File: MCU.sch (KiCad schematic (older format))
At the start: 14 parts

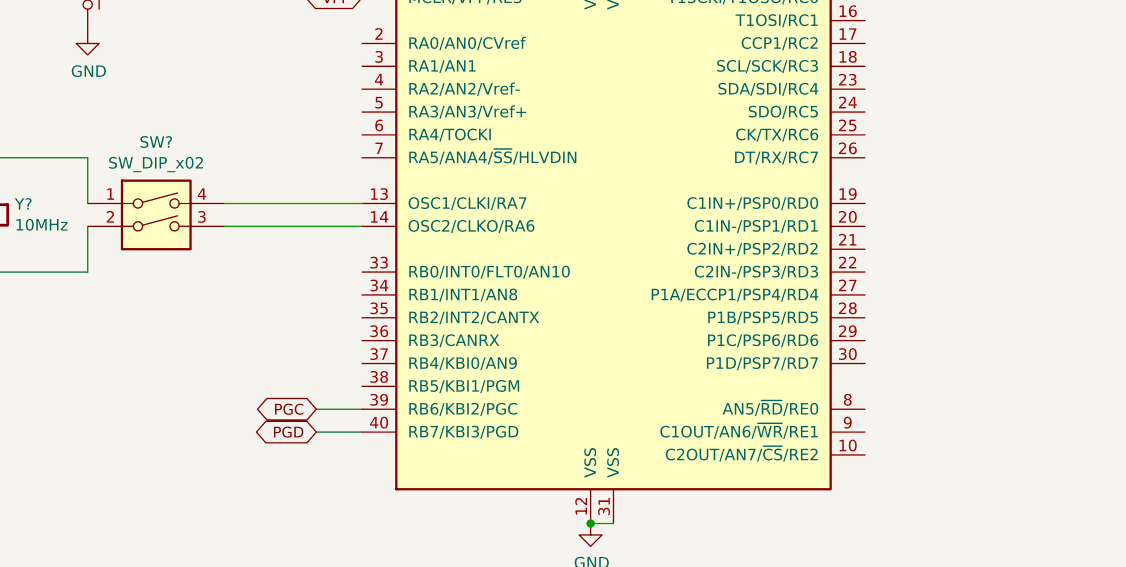
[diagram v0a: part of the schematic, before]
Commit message: LCD Blok Tasarımı
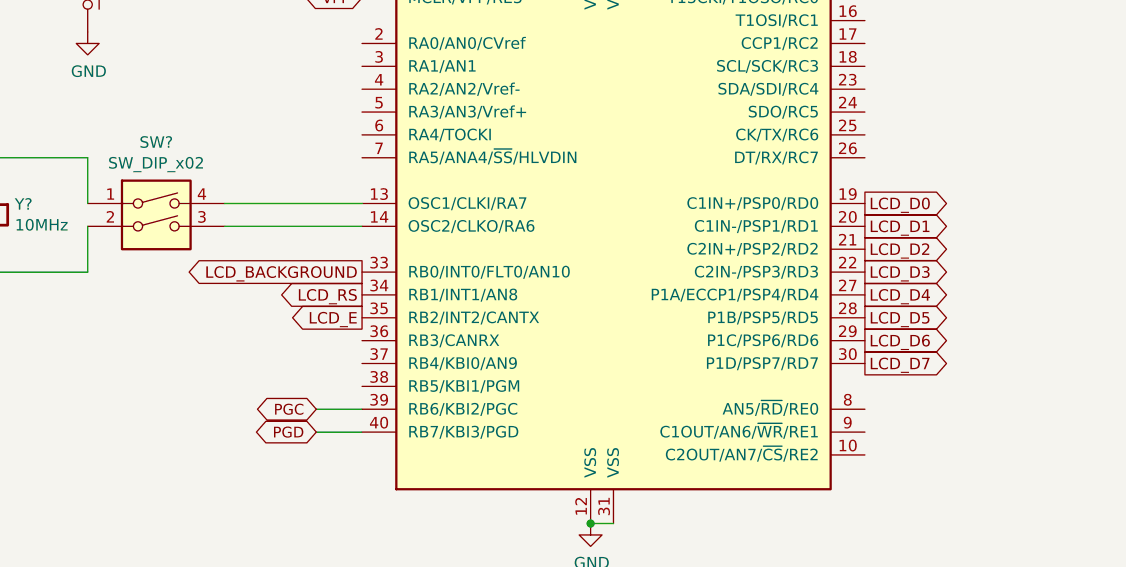
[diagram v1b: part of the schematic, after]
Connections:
- net LCD_D0: now reaches U?.19 (C1IN+/PSP0/RD0)
- net LCD_D1: now reaches U?.20 (C1IN-/PSP1/RD1)
- net LCD_D2: now reaches U?.21 (C2IN+/PSP2/RD2)
- net LCD_D3: now reaches U?.22 (C2IN-/PSP3/RD3)
- net LCD_D4: now reaches U?.27 (P1A/ECCP1/PSP4/RD4)
- net LCD_D5: now reaches U?.28 (P1B/PSP5/RD5)
- net LCD_D6: now reaches U?.29 (P1C/PSP6/RD6)
- net LCD_D7: now reaches U?.30 (P1D/PSP7/RD7)
- net LCD_BACKGROUND: now reaches U?.33 (RB0/INT0/FLT0/AN10)
- net LCD_RS: now reaches U?.34 (RB1/INT1/AN8)
- net LCD_E: now reaches U?.35 (RB2/INT2/CANTX)
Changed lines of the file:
@@
 $Descr A4 11693 8268
 encoding utf-8
-Sheet 2 2
+Sheet 2 3
 Title ""
 Date ""
@@
 	3350 2850 3300 2850
 Connection ~ 3300 2850
+Text GLabel 4500 4350 0    50   Output ~ 0
+LCD_BACKGROUND
+Text GLabel 4500 4450 0    50   Output ~ 0
+LCD_RS
+Text GLabel 4500 4550 0    50   Output ~ 0
+LCD_E
+Text GLabel 6700 4050 2    50   Output ~ 0
+LCD_D0
+Text GLabel 6700 4150 2    50   Output ~ 0
+LCD_D1
+Text GLabel 6700 4250 2    50   Output ~ 0
+LCD_D2
+Text GLabel 6700 4350 2    50   Output ~ 0
+LCD_D3
+Text GLabel 6700 4450 2    50   Output ~ 0
+LCD_D4
+Text GLabel 6700 4550 2    50   Output ~ 0
+LCD_D5
+Text GLabel 6700 4650 2    50   Output ~ 0
+LCD_D6
+Text GLabel 6700 4750 2    50   Output ~ 0
+LCD_D7
 $EndSCHEMATC

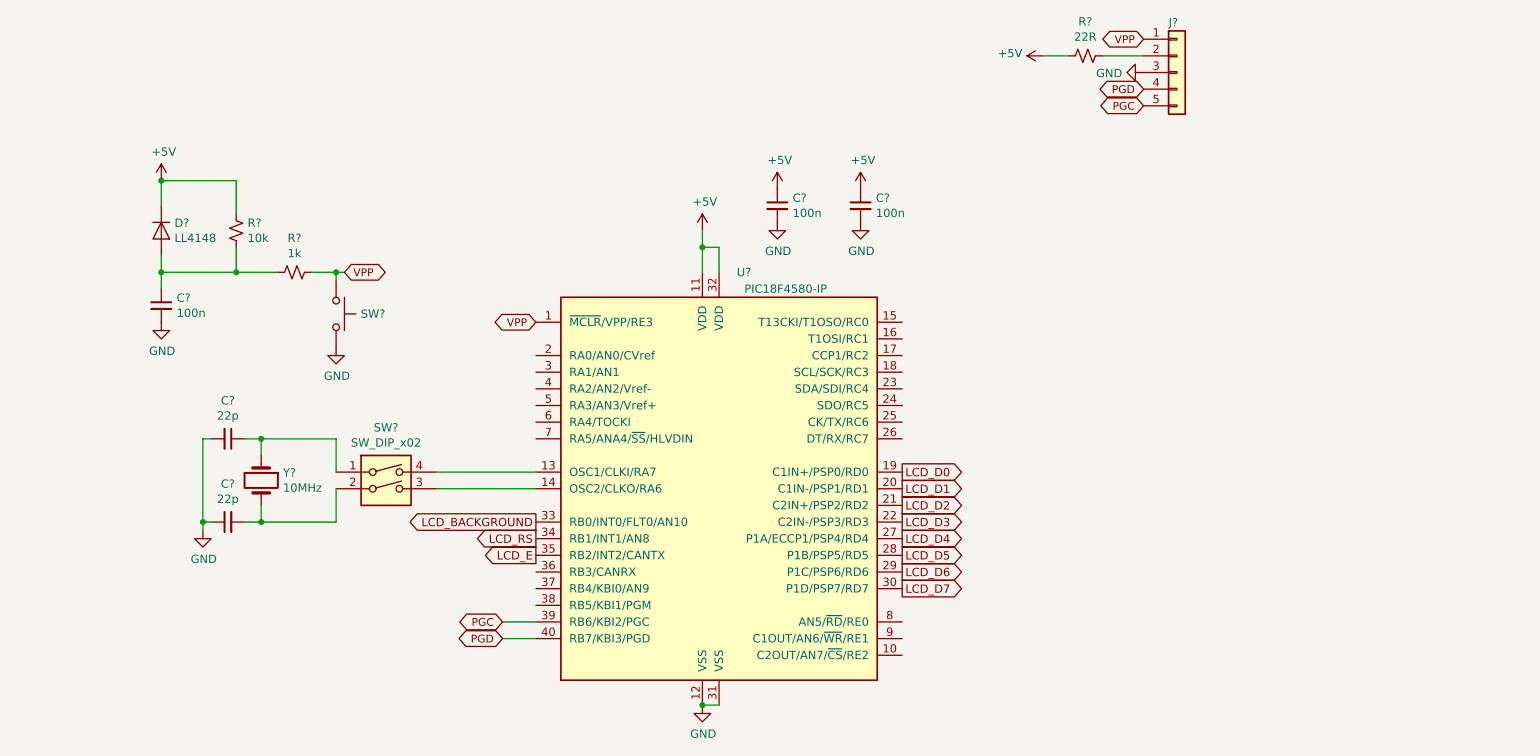
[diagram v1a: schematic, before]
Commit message: LED, ADC, DISPLAY Eklendi
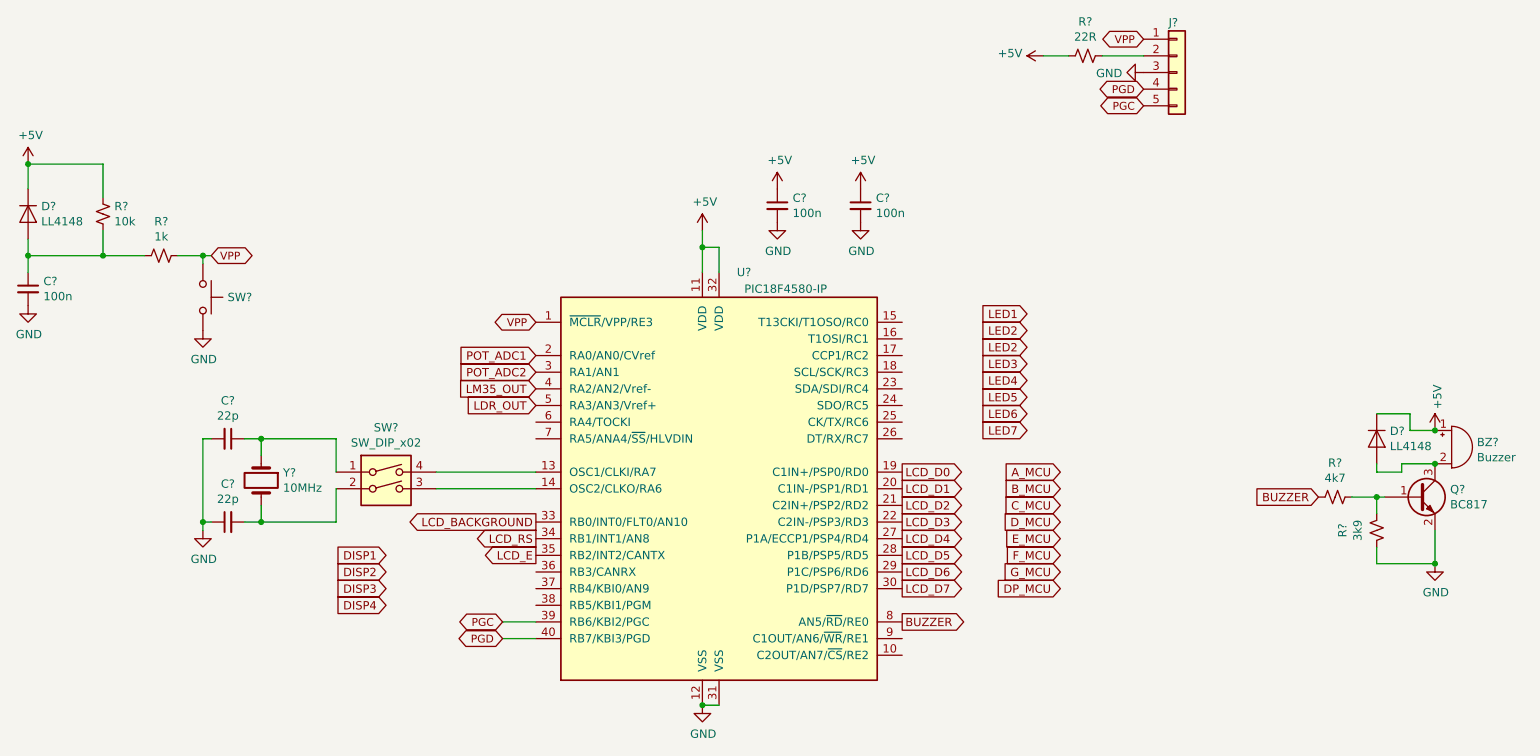
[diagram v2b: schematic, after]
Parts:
- added BZ?: Buzzer, Buzzer_Beeper:MagneticBuzzer_PUI_AT-0927-TT-6-R, symbol Device:Buzzer
- added D?: LL4148, Diode_SMD:D_MiniMELF, symbol Diode:LL4148
- added Q?: BC817, Package_TO_SOT_SMD:SOT-23, symbol Transistor_BJT:BC817
- added R?: 4k7, Resistor_SMD:R_0805_2012Metric, symbol Device:R_Small_US
- added R?: 3k9, Resistor_SMD:R_0805_2012Metric, symbol Device:R_Small_US
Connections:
- net +5V: now also BZ?.1 (-), D?.1 (K)
- net GND: now also Q?.2 (E), R?.1
- net POT_ADC1: now reaches U?.2 (RA0/AN0/CVref)
- net POT_ADC2: now reaches U?.3 (RA1/AN1)
- net LM35_OUT: now reaches U?.4 (RA2/AN2/Vref-)
- net LDR_OUT: now reaches U?.5 (RA3/AN3/Vref+)
- net BUZZER: now reaches U?.8 (AN5/~RD~/RE0)
- net BUZZER: now also R?.2
- new net: BZ?.2 (+), D?.2 (A), Q?.3 (C)
- new net: Q?.1 (B), R?.1, R?.2
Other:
- moved on the sheet: C?, D?, R?, SW?
